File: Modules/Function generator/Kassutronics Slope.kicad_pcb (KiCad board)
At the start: 2 copper layers, 185.6 x 128.5 mm, 151 parts, among them J1 PJ301M-12, J10 Conn_01x08_Female, J11 Conn_01x08_Male, J12 Conn_01x05_Female, J13 Conn_01x05_Male, J14 Conn_01x06_Female, J15 Conn_01x06_Male, J2 PJ301M-12, J3 PJ301M-12, J4 PJ301M-12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

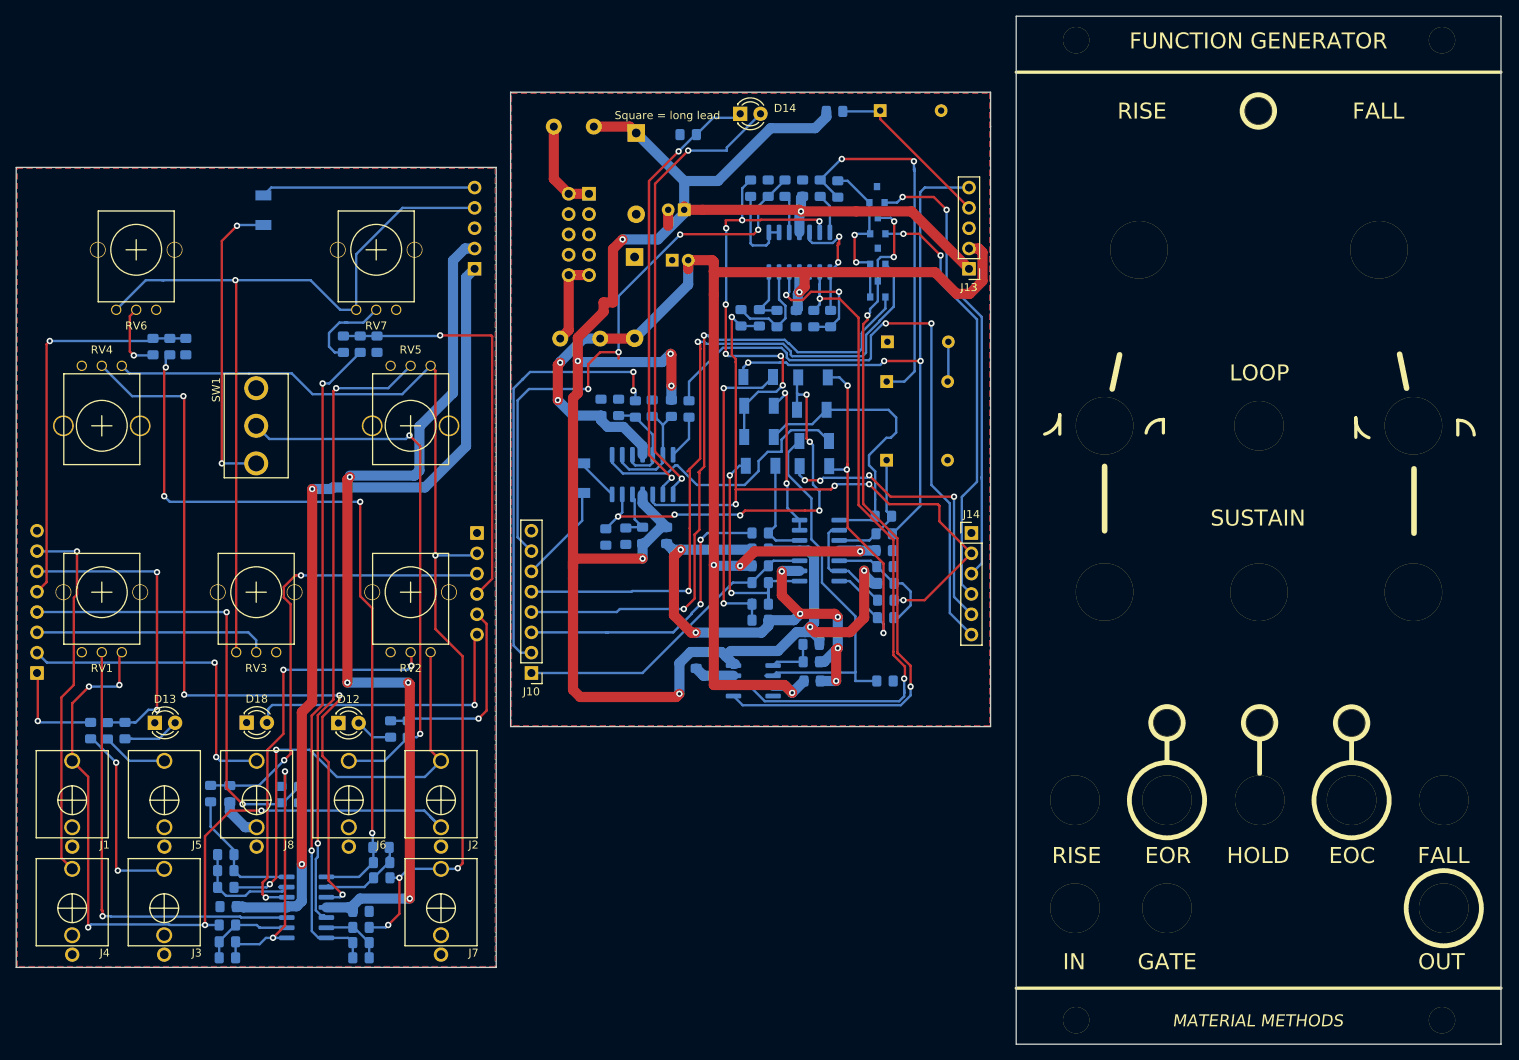
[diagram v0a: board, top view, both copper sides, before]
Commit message: Function generator UI tweaks
Tweaked Function generator knob placement for more finger space.
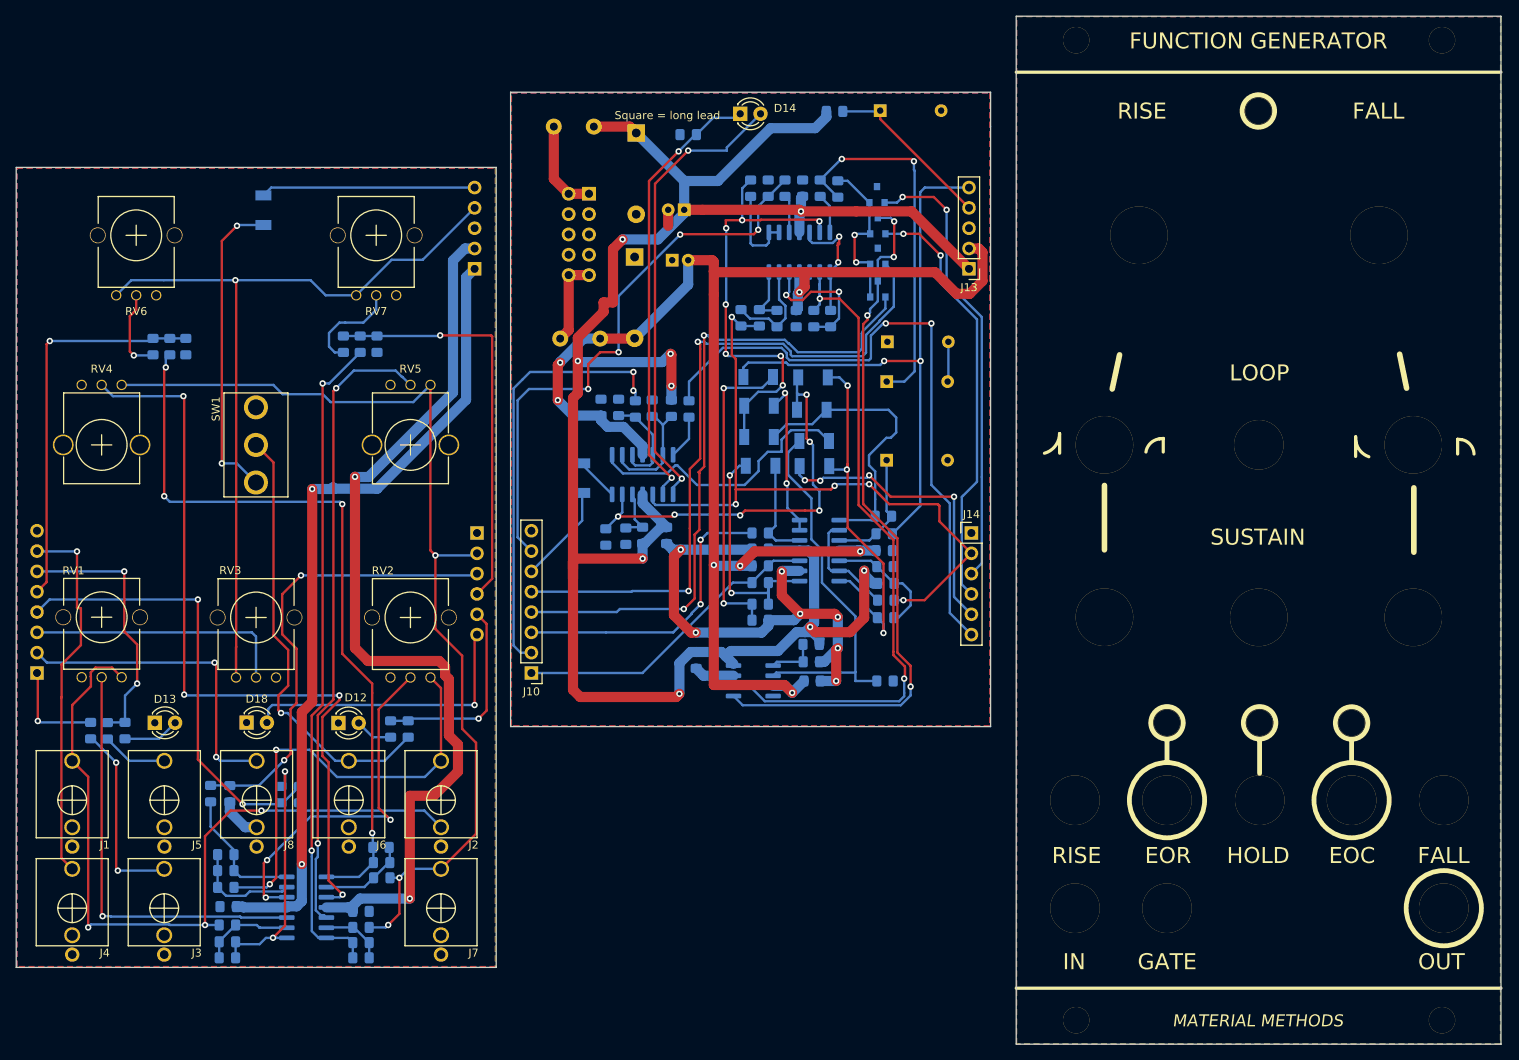
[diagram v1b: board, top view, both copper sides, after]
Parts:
- moved RV2 3.16 mm to (79.3, 86.3)
- moved RV3 3.16 mm to (60.0, 86.3)
- moved ? 3.15 mm to (204.6, 86.2)
- moved ? 3.15 mm to (185.3, 86.2)
- moved ? 3.15 mm to (166.0, 86.2)
- moved RV1 3.13 mm to (40.7, 86.2)
- moved SW1 2.39 mm to (60.0, 64.7)
- moved RV4 2.39 mm to (40.7, 64.7)
- moved RV5 2.39 mm to (79.3, 64.7)
- moved ? 2.38 mm to (166.0, 64.7)
- moved ? 2.38 mm to (204.6, 64.7)
- moved ? 2.38 mm to (185.3, 64.7)
- moved ? 1.82 mm to (170.3, 38.5)
- moved ? 1.82 mm to (200.3, 38.5)
- moved RV6 1.81 mm to (45.0, 38.5)
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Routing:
- net EOC_t: track 68.2 -> 55.4 mm, vias 2 -> 1
- net EOR_out_t: track 39.1 -> 33.3 mm
- net /Fall_CV_pot: track 50.3 -> 45.5 mm
- net +12V: track 370.2 -> 366.3 mm
- net /Rise_CV_in: track 101.6 -> 98.0 mm, vias 5 -> 3
- net SUSTAIN_t: track 29.3 -> 32.7 mm
- net VREF_t: track 104.0 -> 100.6 mm
- net OUT_t: track 129.5 -> 126.2 mm, vias 4 -> 3
- net /Rise_CV_pot: track 56.2 -> 53.0 mm
- net /Fall_CV_in: track 58.8 -> 55.6 mm
- net -12V: track 301.3 -> 303.4 mm, vias 11 -> 9
- net /Rise_pot: track 8.67 -> 10.5 mm
- net /Fall_pot: track 11.2 -> 12.7 mm
- net Net-(C4-Pad1): track 95.2 -> 93.7 mm
- net Net-(C2-Pad2): track 14.6 -> 13.6 mm
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- added copper zone on B.Cu, net (none)
- added copper zone on F.Cu, net (none)
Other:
- net class Default removed
- net class Power removed

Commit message: Function generator: added pulldown resistors to gate outputs
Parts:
- added R55: 470k, Eurocad:R_0805_2012Metric_Pad1.15x1.40mm_HandSolder_smallText, B.Cu at (48.0, 75.5)
- added R56: 470k, Eurocad:R_0805_2012Metric_Pad1.15x1.40mm_HandSolder_smallText, B.Cu at (81.3, 100.2)
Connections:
- J1 pad 2: (no net) -> unconnected-(J1-Pad2)
- J3 pad 2: (no net) -> unconnected-(J3-Pad2)
- J4 pad 2: (no net) -> unconnected-(J4-Pad2)
- J5 pad 2: (no net) -> unconnected-(J5-Pad2)
- J6 pad 2: (no net) -> unconnected-(J6-Pad2)
- J7 pad 2: (no net) -> unconnected-(J7-Pad2)
- SW1 pad 1: (no net) -> unconnected-(SW1-Pad1)
- U4 pad 8: (no net) -> unconnected-(U4-Pad8)
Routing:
- net EOR_out_t: track 33.3 -> 41.4 mm
